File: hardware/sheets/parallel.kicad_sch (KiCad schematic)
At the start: 27 parts, among them J1 DB25_Pins, U1 74LVC574A, U10 74HC32, U11 74HC32, U12 74HC00, U2 74LVC574A, U3 74LVC244A, U4 74LVC245A, U5 74LVC244A, U6 74HC138, U9 74AHC14

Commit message: parallel: fold U11's lone OR gate into U12's spare NANDs
U11 (74HC32) survived the decode centralization carrying one gate,
~{RD_CTRL} = ~{SEL_CTRL} | ~{IOR}. Rebuilt as OR-from-NAND on U12's
three spares (two input inverters + one combine); the ~25ns of added
gate delay is noise in an ~840ns ISA read cycle. U12 now 4/4 used,
LPT sheet down to 9 ICs; board 452 comps / 91 ICs.

Co-Authored-By: Claude Fable 5 <noreply@anthropic.com>
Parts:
- removed C10: 100nF, Capacitor_SMD:C_0603_1608Metric, symbol Device:C
- removed U11: 74HC32, Package_SO:SOIC-14_3.9x8.7mm_P1.27mm, symbol mini-xt:74HCT32
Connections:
- net GND: no longer U12.10 (P10), U12.12 (P12), U12.13 (P13), U12.4 (P4), U12.5 (P5), U12.9 (P9)
- net ~{IOR}: now also U12.10 (P10), U12.9 (P9)
- net ~{RD_CTRL}: now also U12.11 (P11)
- net ~{SEL_CTRL}: now also U12.4 (P4), U12.5 (P5)
- net SEL_CTRL_POS: now reaches U12.6 (P6)
- net SEL_CTRL_POS: now also U12.12 (P12)
- net IOR_POS: now reaches U12.8 (P8)
- net IOR_POS: now also U12.13 (P13)
- no-connect marks 17 -> 11

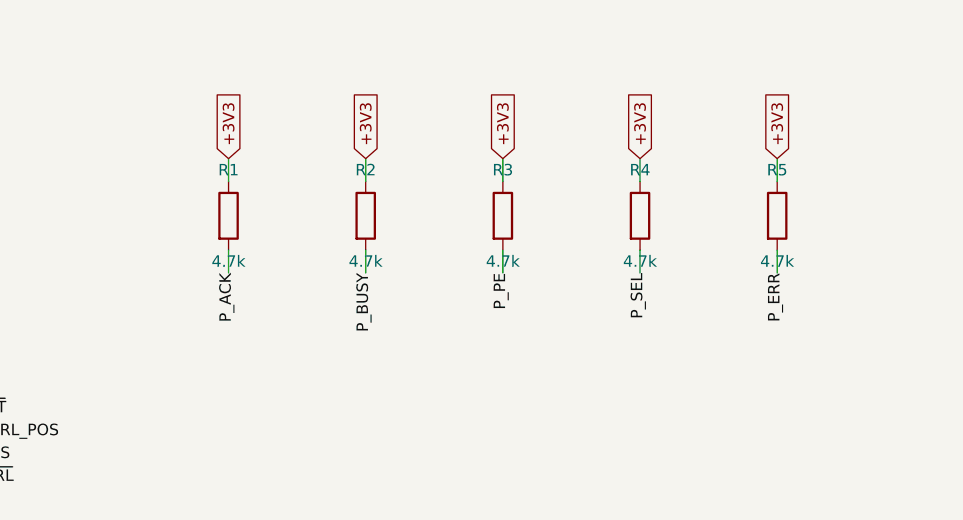
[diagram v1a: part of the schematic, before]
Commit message: Passives: basic-library audit + 4x resistor-array pull consolidation
Audit: every discrete R/C value was already JLC basic except the ferrite
beads -- swapped to basic Murata BLM18PG121SN1D (C14709, 120R@100MHz,
same family/role). The 100uF electrolytic and buck inductor stay
extended (zero fee-free parts exist in those subcategories). Pruned the
orphaned 5V-era 47nF/330nF MAX3241 cap entries.

Pull consolidation: 65 discrete 10k/4.7k rail pulls across 8 sheets
collapse into 18 basic 4-element isolated arrays (4D03WGJ0103T5E /
4D03WGJ0472T5E, element k = pins k/9-k; new mxbus.r_pack4 helper).
Isolated elements let packs mix rails; every net keeps its exact rail
and semantics (verified element-by-element in the netlist). RC/divider/
series/I2C resistors stay discrete. Board 452 -> 406 components; also
de-risks the sole basic 10k 0603 line (0 stock at audit). Audit
recorded in jlcpcb-sourcing.md.

Co-Authored-By: Claude Fable 5 <noreply@anthropic.com>
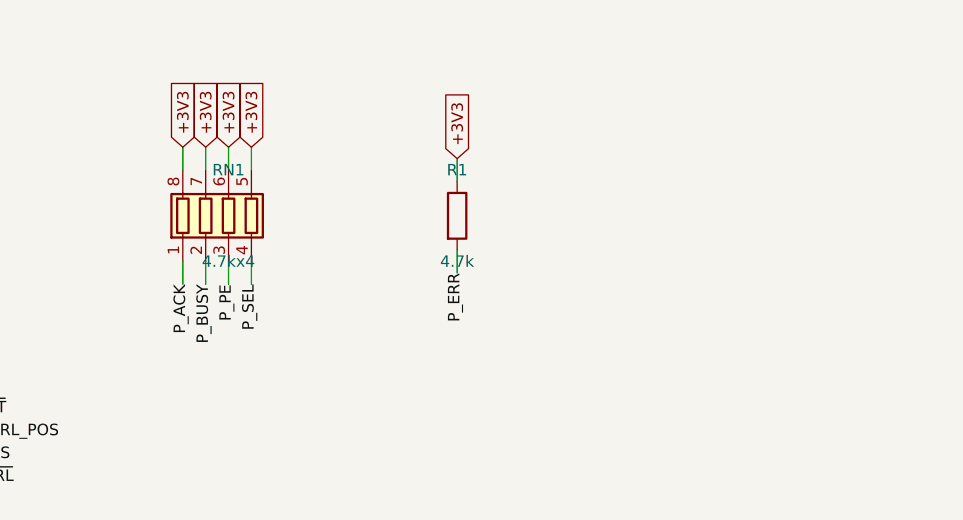
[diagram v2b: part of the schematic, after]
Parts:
- removed R2, R3, R4, R5: 4.7k, Resistor_SMD:R_0603_1608Metric, symbol Device:R
- added R1: 4.7k, Resistor_SMD:R_0603_1608Metric, symbol Device:R
- RN1: renamed from R1; value 4.7k -> 4.7kx4; footprint Resistor_SMD:R_0603_1608Metric -> Resistor_SMD:R_Array_Convex_4x0603; symbol Device:R -> Device:R_Pack04; LCSC Part Num C23162 -> C1980
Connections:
- net +3V3: now also RN1.5 (R4.2), RN1.6 (R3.2), RN1.7 (R2.2), RN1.8 (R1.2), R1.1; no longer RN1.1
- net P_ACK: now also RN1.1 (R1.1); no longer RN1.2
- net P_BUSY: now also RN1.2 (R2.1)
- net P_ERR: now also R1.2
- net P_PE: now also RN1.3 (R3.1)
- net P_SEL: now also RN1.4 (R4.1)

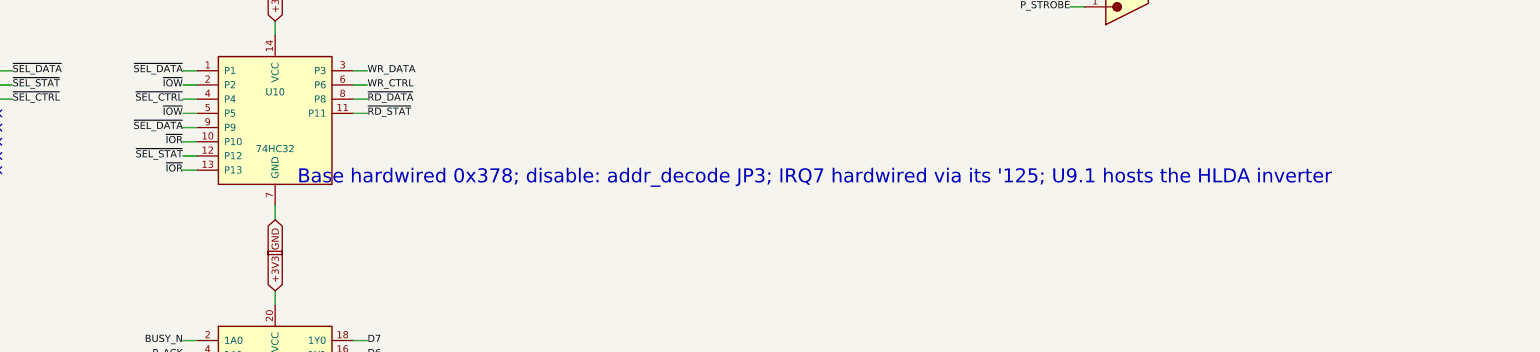
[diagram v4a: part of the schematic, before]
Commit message: Expansion port: 50-pin header, port DMA channel, dev cards deleted
Two waves of the 2026-07-14/15 expansion-port rework (the first was
uncommitted): the IRQ-scan collapse to one '165 + '32 OR rank with
ISA-card DMA removed outright, then the port redesign that brings one
DMA channel back:

- isa_conn: 60-pin (2x30, PicoGUS-standard layout) -> 50-pin (2x25,
  project-private pinout; 50-way IDC is far easier to source). OSC and
  ~REFRESH dropped to fit (no on-board consumer / no DRAM refresh; the
  planned ISA backplane board re-creates both for period cards).
- Port DMA: EXT_DRQ rides the sidecar inbound '244 + U12 '165 spare D6
  lane (zero GPIO); ~EXT_DACK = GPIO47 (freed by ~REFRESH) out through
  the strobe '244. Separate nets from the internal PicoGUS pair, so a
  port card never sees the on-board acknowledge.
- DRQ1/~DACK1 renamed DRQ/~DACK (ch2/3 long retired); DRQ2/3 +
  ~DACK2/3 removed from the mxbus contract.
- card_video + card_isatest deleted (sheets, hardware/cards/,
  build_cards()); superseded by the backplane plan. History has them.
- Connector parts: IDE header -> shrouded 2x20 IDC box (C9138, keypin
  20 NC'd); expansion port -> 90-degree 2x25 female socket (C21262364);
  addr_decode's five disable jumpers folded into ONE fixed 2x5 block
  JP1 (C492422), positions JP1.1-JP1.5 = COM1/COM2/LPT/IDE/VID.

ERC 0/0, check_parts 0 problems; docs/notes updated throughout.

Co-Authored-By: Claude Fable 5 <noreply@anthropic.com>
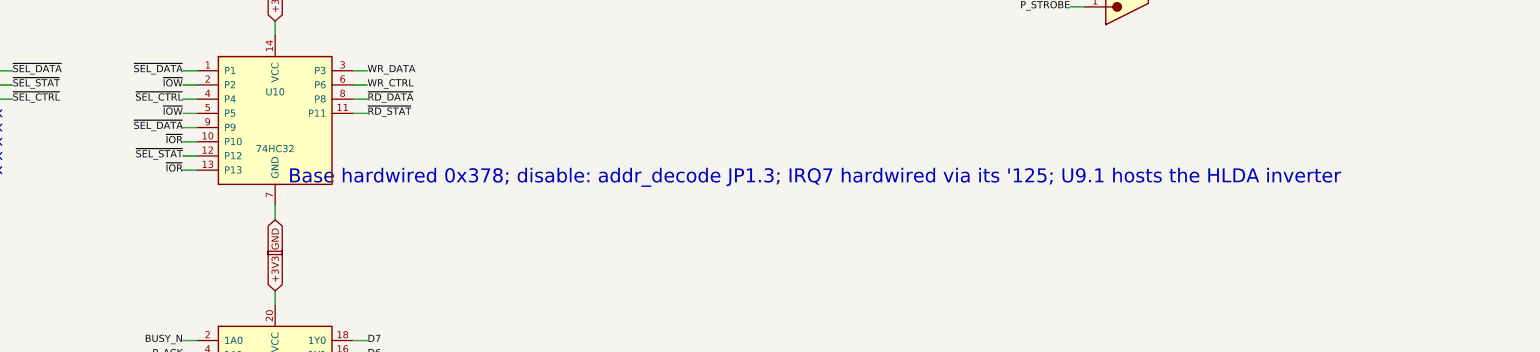
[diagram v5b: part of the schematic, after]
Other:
- note added: "Base hardwired 0x378; disable: addr_decode JP1.3; IRQ7 hardwired via its '125; U9.1 hosts the HLDA inverter"
- note removed: "Base hardwired 0x378; disable: addr_decode JP3; IRQ7 hardwired via its '125; U9.1 hosts the HLDA inverter"
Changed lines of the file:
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@@
 		)
 	)
-	(text "Base hardwired 0x378; disable: addr_decode JP3; IRQ7 hardwired via its '125; U9.1 hosts the HLDA inverter"
+	(text "Base hardwired 0x378; disable: addr_decode JP1.3; IRQ7 hardwired via its '125; U9.1 hosts the HLDA inverter"
 		(at 299.72 187.96 0)
 		(effects
@@
 		(instances
 			(project "mini-xt"
-				(path "/26736c46-8b40-5460-874f-03596d17270c/249151b3-3e1d-5297-b42d-94378272ed2e"
+				(path "/26736c46-8b40-5460-874f-03596d17270c/b2a44275-f07d-52f2-87a9-605a39aa65cd"
 					(reference "U609")
 					(unit 1)
@@
 		(instances
 			(project "mini-xt"
-				(path "/26736c46-8b40-5460-874f-03596d17270c/249151b3-3e1d-5297-b42d-94378272ed2e"
+				(path "/26736c46-8b40-5460-874f-03596d17270c/b2a44275-f07d-52f2-87a9-605a39aa65cd"
 					(reference "U612")
 					(unit 1)
@@
 		(instances
 			(project "mini-xt"
-				(path "/26736c46-8b40-5460-874f-03596d17270c/249151b3-3e1d-5297-b42d-94378272ed2e"
+				(path "/26736c46-8b40-5460-874f-03596d17270c/b2a44275-f07d-52f2-87a9-605a39aa65cd"
 					(reference "U606")
 					(unit 1)
@@
 		(instances
 			(project "mini-xt"
-				(path "/26736c46-8b40-5460-874f-03596d17270c/249151b3-3e1d-5297-b42d-94378272ed2e"
+				(path "/26736c46-8b40-5460-874f-03596d17270c/b2a44275-f07d-52f2-87a9-605a39aa65cd"
 					(reference "U610")
 					(unit 1)
@@
 		(instances
 			(project "mini-xt"
-				(path "/26736c46-8b40-5460-874f-03596d17270c/249151b3-3e1d-5297-b42d-94378272ed2e"
+				(path "/26736c46-8b40-5460-874f-03596d17270c/b2a44275-f07d-52f2-87a9-605a39aa65cd"
 					(reference "U601")
 					(unit 1)
@@
 		(instances
 			(project "mini-xt"
-				(path "/26736c46-8b40-5460-874f-03596d17270c/249151b3-3e1d-5297-b42d-94378272ed2e"
+				(path "/26736c46-8b40-5460-874f-03596d17270c/b2a44275-f07d-52f2-87a9-605a39aa65cd"
 					(reference "U604")
 					(unit 1)
@@
 		(instances
 			(project "mini-xt"
-				(path "/26736c46-8b40-5460-874f-03596d17270c/249151b3-3e1d-5297-b42d-94378272ed2e"
+				(path "/26736c46-8b40-5460-874f-03596d17270c/b2a44275-f07d-52f2-87a9-605a39aa65cd"
 					(reference "U602")
 					(unit 1)
@@
 		(instances
 			(project "mini-xt"
-				(path "/26736c46-8b40-5460-874f-03596d17270c/249151b3-3e1d-5297-b42d-94378272ed2e"
+				(path "/26736c46-8b40-5460-874f-03596d17270c/b2a44275-f07d-52f2-87a9-605a39aa65cd"
 					(reference "U605")
 					(unit 1)
@@
 		(instances
 			(project "mini-xt"
-				(path "/26736c46-8b40-5460-874f-03596d17270c/249151b3-3e1d-5297-b42d-94378272ed2e"
+				(path "/26736c46-8b40-5460-874f-03596d17270c/b2a44275-f07d-52f2-87a9-605a39aa65cd"
 					(reference "U603")
 					(unit 1)
@@
 		(instances
 			(project "mini-xt"
-				(path "/26736c46-8b40-5460-874f-03596d17270c/249151b3-3e1d-5297-b42d-94378272ed2e"
+				(path "/26736c46-8b40-5460-874f-03596d17270c/b2a44275-f07d-52f2-87a9-605a39aa65cd"
 					(reference "J601")
 					(unit 1)
@@
 		(instances
 			(project "mini-xt"
-				(path "/26736c46-8b40-5460-874f-03596d17270c/249151b3-3e1d-5297-b42d-94378272ed2e"
+				(path "/26736c46-8b40-5460-874f-03596d17270c/b2a44275-f07d-52f2-87a9-605a39aa65cd"
 					(reference "RN601")
 					(unit 1)
@@
 		(instances
 			(project "mini-xt"
-				(path "/26736c46-8b40-5460-874f-03596d17270c/249151b3-3e1d-5297-b42d-94378272ed2e"
+				(path "/26736c46-8b40-5460-874f-03596d17270c/b2a44275-f07d-52f2-87a9-605a39aa65cd"
 					(reference "R601")
 					(unit 1)
@@
 		(instances
 			(project "mini-xt"
-				(path "/26736c46-8b40-5460-874f-03596d17270c/249151b3-3e1d-5297-b42d-94378272ed2e"
+				(path "/26736c46-8b40-5460-874f-03596d17270c/b2a44275-f07d-52f2-87a9-605a39aa65cd"
 					(reference "C601")
 					(unit 1)
@@
 		(instances
 			(project "mini-xt"
-				(path "/26736c46-8b40-5460-874f-03596d17270c/249151b3-3e1d-5297-b42d-94378272ed2e"
+				(path "/26736c46-8b40-5460-874f-03596d17270c/b2a44275-f07d-52f2-87a9-605a39aa65cd"
 					(reference "C602")
 					(unit 1)
@@
 		(instances
 			(project "mini-xt"
-				(path "/26736c46-8b40-5460-874f-03596d17270c/249151b3-3e1d-5297-b42d-94378272ed2e"
+				(path "/26736c46-8b40-5460-874f-03596d17270c/b2a44275-f07d-52f2-87a9-605a39aa65cd"
 					(reference "C603")
 					(unit 1)
@@
 		(instances
 			(project "mini-xt"
-				(path "/26736c46-8b40-5460-874f-03596d17270c/249151b3-3e1d-5297-b42d-94378272ed2e"
+				(path "/26736c46-8b40-5460-874f-03596d17270c/b2a44275-f07d-52f2-87a9-605a39aa65cd"
 					(reference "C604")
 					(unit 1)
@@
 		(instances
 			(project "mini-xt"
-				(path "/26736c46-8b40-5460-874f-03596d17270c/249151b3-3e1d-5297-b42d-94378272ed2e"
+				(path "/26736c46-8b40-5460-874f-03596d17270c/b2a44275-f07d-52f2-87a9-605a39aa65cd"
 					(reference "C605")
 					(unit 1)
@@
 		(instances
 			(project "mini-xt"
-				(path "/26736c46-8b40-5460-874f-03596d17270c/249151b3-3e1d-5297-b42d-94378272ed2e"
+				(path "/26736c46-8b40-5460-874f-03596d17270c/b2a44275-f07d-52f2-87a9-605a39aa65cd"
 					(reference "C606")
 					(unit 1)
@@
 		(instances
 			(project "mini-xt"
-				(path "/26736c46-8b40-5460-874f-03596d17270c/249151b3-3e1d-5297-b42d-94378272ed2e"
+				(path "/26736c46-8b40-5460-874f-03596d17270c/b2a44275-f07d-52f2-87a9-605a39aa65cd"
 					(reference "C607")
 					(unit 1)
@@
 		(instances
 			(project "mini-xt"
-				(path "/26736c46-8b40-5460-874f-03596d17270c/249151b3-3e1d-5297-b42d-94378272ed2e"
+				(path "/26736c46-8b40-5460-874f-03596d17270c/b2a44275-f07d-52f2-87a9-605a39aa65cd"
 					(reference "C608")
 					(unit 1)
@@
 		(instances
 			(project "mini-xt"
-				(path "/26736c46-8b40-5460-874f-03596d17270c/249151b3-3e1d-5297-b42d-94378272ed2e"
+				(path "/26736c46-8b40-5460-874f-03596d17270c/b2a44275-f07d-52f2-87a9-605a39aa65cd"
 					(reference "C609")
 					(unit 1)
@@
 		(instances
 			(project "mini-xt"
-				(path "/26736c46-8b40-5460-874f-03596d17270c/249151b3-3e1d-5297-b42d-94378272ed2e"
+				(path "/26736c46-8b40-5460-874f-03596d17270c/b2a44275-f07d-52f2-87a9-605a39aa65cd"
 					(reference "C614")
 					(unit 1)

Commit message: Sourcing: 10k pulls to 0805 basic C17414, DB25 to socket footprint
parts.py swaps propagate through the regenerated sheets/netlist; LCSC
price cache and jlcpcb-sourcing notes updated to match.

Co-Authored-By: Claude Fable 5 <noreply@anthropic.com>
Claude-Session: https://claude.ai/code/session_01Y7zRS7ikVENkjZFFBcegCP
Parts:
- J1: footprint Connector_Dsub:DSUB-25_Pins_Horizontal_P2.77x2.84mm_EdgePinOffset9.90mm_Housed_MountingHolesOffset11.32mm -> Connector_Dsub:DSUB-25_Socket_Horizontal_P2.77x2.84mm_EdgePinOffset9.90mm_Housed_MountingHolesOffset11.32mm; LCSC Part Num C5400534 -> C190083
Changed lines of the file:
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@@
 			)
 		)
-		(property "Footprint" "Connector_Dsub:DSUB-25_Pins_Horizontal_P2.77x2.84mm_EdgePinOffset9.90mm_Housed_MountingHolesOffset11.32mm"
+		(property "Footprint" "Connector_Dsub:DSUB-25_Socket_Horizontal_P2.77x2.84mm_EdgePinOffset9.90mm_Housed_MountingHolesOffset11.32mm"
 			(at 355.6 127 0)
 			(effects
@@
 			)
 		)
-		(property "LCSC Part Num" "C5400534"
+		(property "LCSC Part Num" "C190083"
 			(at 355.6 127 0)
 			(effects
